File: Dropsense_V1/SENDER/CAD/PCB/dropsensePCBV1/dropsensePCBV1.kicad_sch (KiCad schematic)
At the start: 26 parts, among them J1 Micro_SD_Card_Det_Hirose_DM3AT, J2 USB_B_Micro, J3 battery socket, SW1 SW_Push, SW2 SW_Push, U1 ESP32-S3-WROOM-1, U2 MPU-6050, U3 TP4056-42-ESOP8, U4 ME6211C10M5

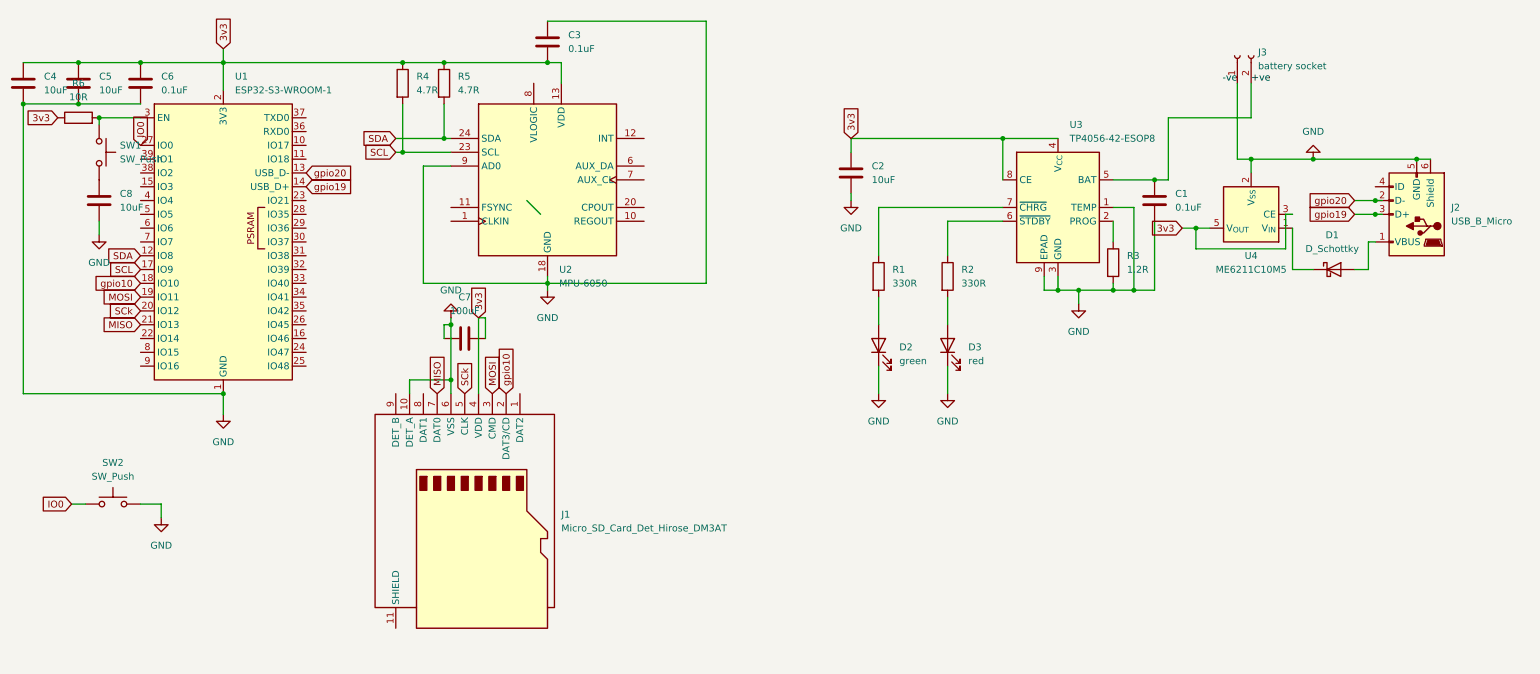
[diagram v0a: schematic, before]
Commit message: PCB improvement
updated and polished both the pcbs of the sender and reciever mainly woked on moving viases away from smd components
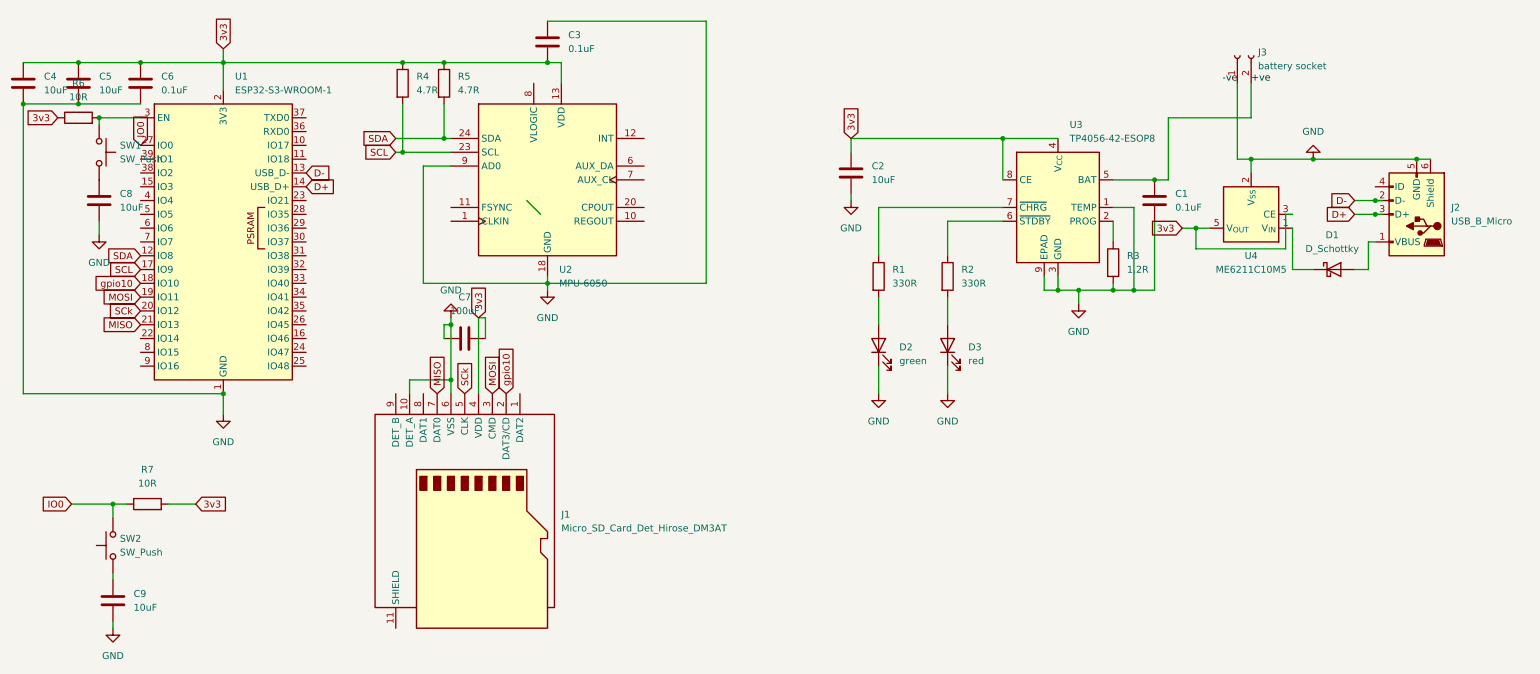
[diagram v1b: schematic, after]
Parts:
- added C9: 10uF, Capacitor_SMD:C_0805_2012Metric, symbol Device:C
- added R7: 10R, Resistor_SMD:R_0805_2012Metric, symbol Device:R
- D1: footprint Diode_SMD:D_SMA -> Diode_SMD:D_0805_2012Metric
- J3: footprint Connector_PinHeader_2.54mm:PinHeader_1x02_P2.54mm_Vertical -> Connector_JST:JST_PH_B2B-PH-K_1x02_P2.00mm_Vertical
- R1, R2, R3, R4, R5, R6: footprint Resistor_SMD:R_0201_0603Metric -> Resistor_SMD:R_0805_2012Metric
- SW1, SW2: footprint Button_Switch_SMD:Nidec_Copal_CAS-120A -> Button_Switch_THT:SW_PUSH_6mm_H4.3mm
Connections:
- net 3v3: now also R7.2
- net GND: now also C9.2; no longer SW2.2
- net IO0: now also SW2.2, R7.1; no longer SW2.1
- net gpio19 renamed D+
- net gpio20 renamed D-
- new net: C9.1, SW2.1
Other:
- moved on the sheet: SW2
